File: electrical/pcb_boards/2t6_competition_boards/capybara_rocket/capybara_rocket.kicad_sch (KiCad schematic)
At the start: 77 parts, among them J1 3.6V Battery, J10 Elevator, J11 SparkFun MAX-M10S, J12 Aileron 1, J13 Aileron 2, J14 Ground Camera, J15 Payload Camera, J16 DC Motor, J2 1.2V Battery, J3 3.6V Switch, J4 1.2V Switch, J5 LED, J6 NC, J7 CC, J8 VL53L1-SATEL, J9 Egg, U1 NE555P, U10 DRV8212DRLR, U11 STM32 NUCLEO-G431KB, U12 SN74LVC1G04DBVR, U13 SparkFun XBee Explorer, U2 DS1307+, U3 Adafruit BNO085, U4 LTC3536, U5 MP3414, U6 Adafruit BMP581, U7 INA219, U8 MAX756CPA+, U9 EEPROM, Y1 AB38T-32.768KHZ

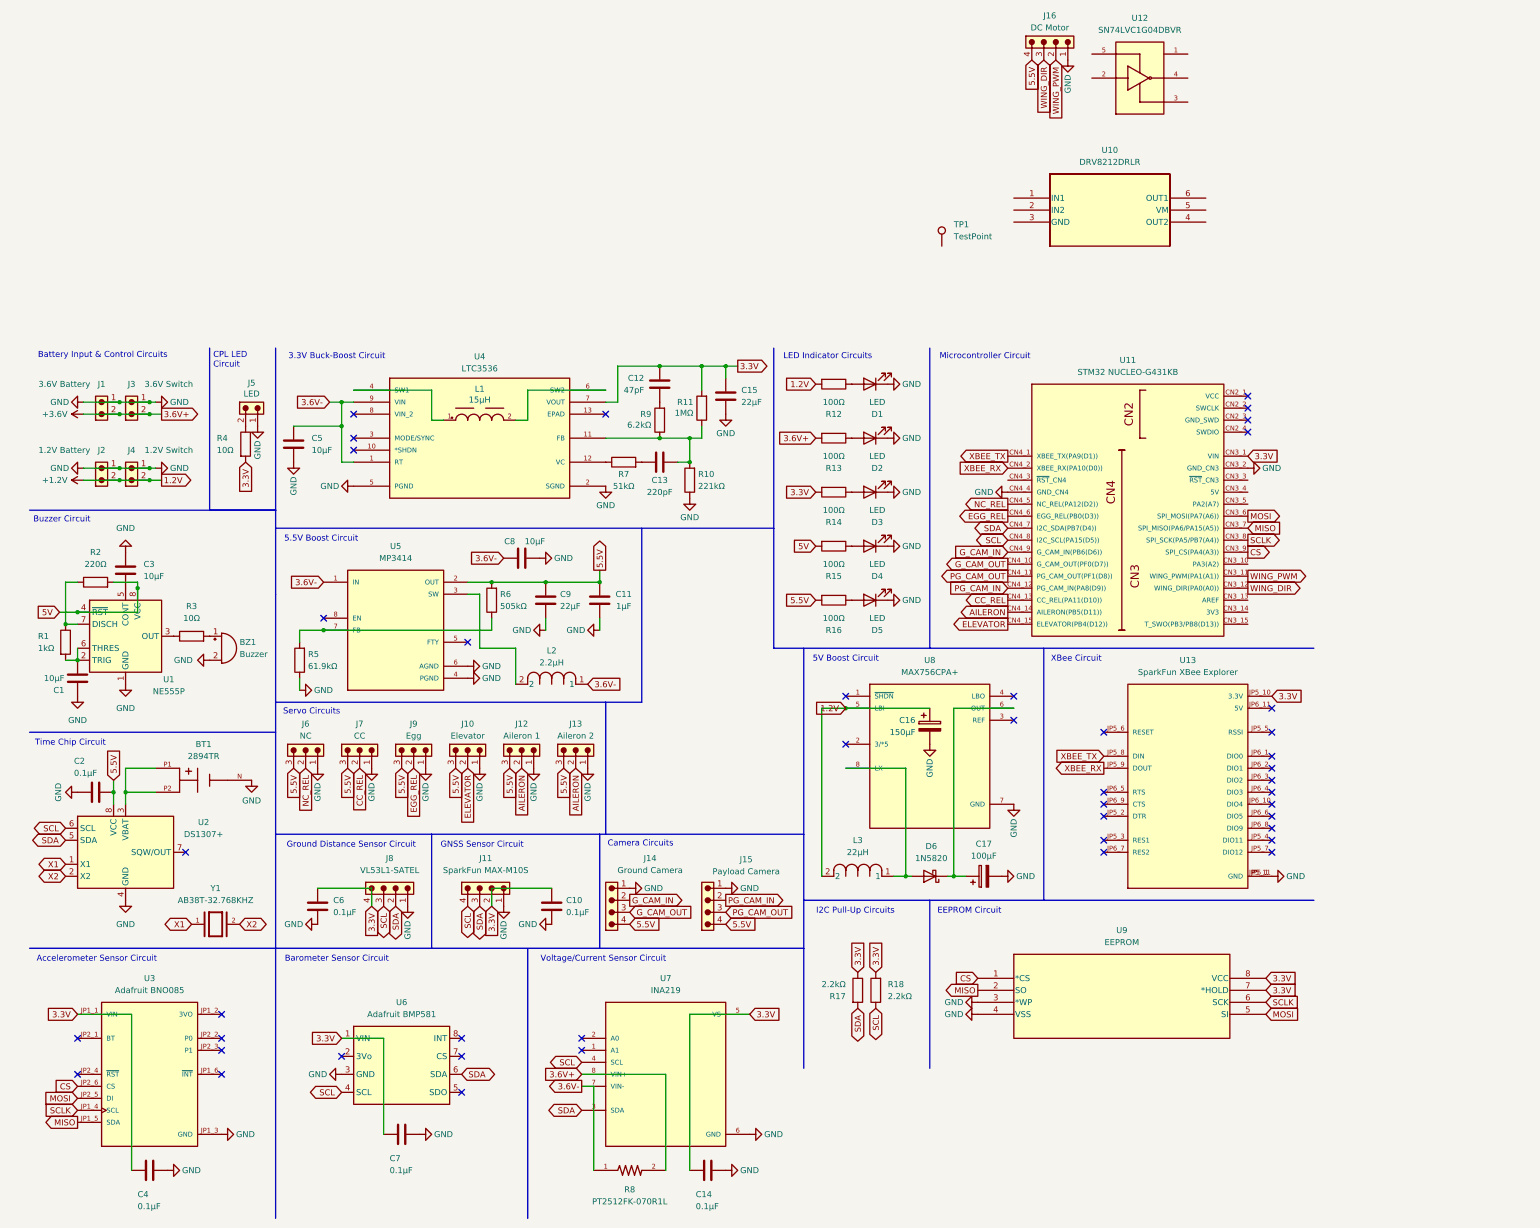
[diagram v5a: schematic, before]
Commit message: Completed CPL schematic
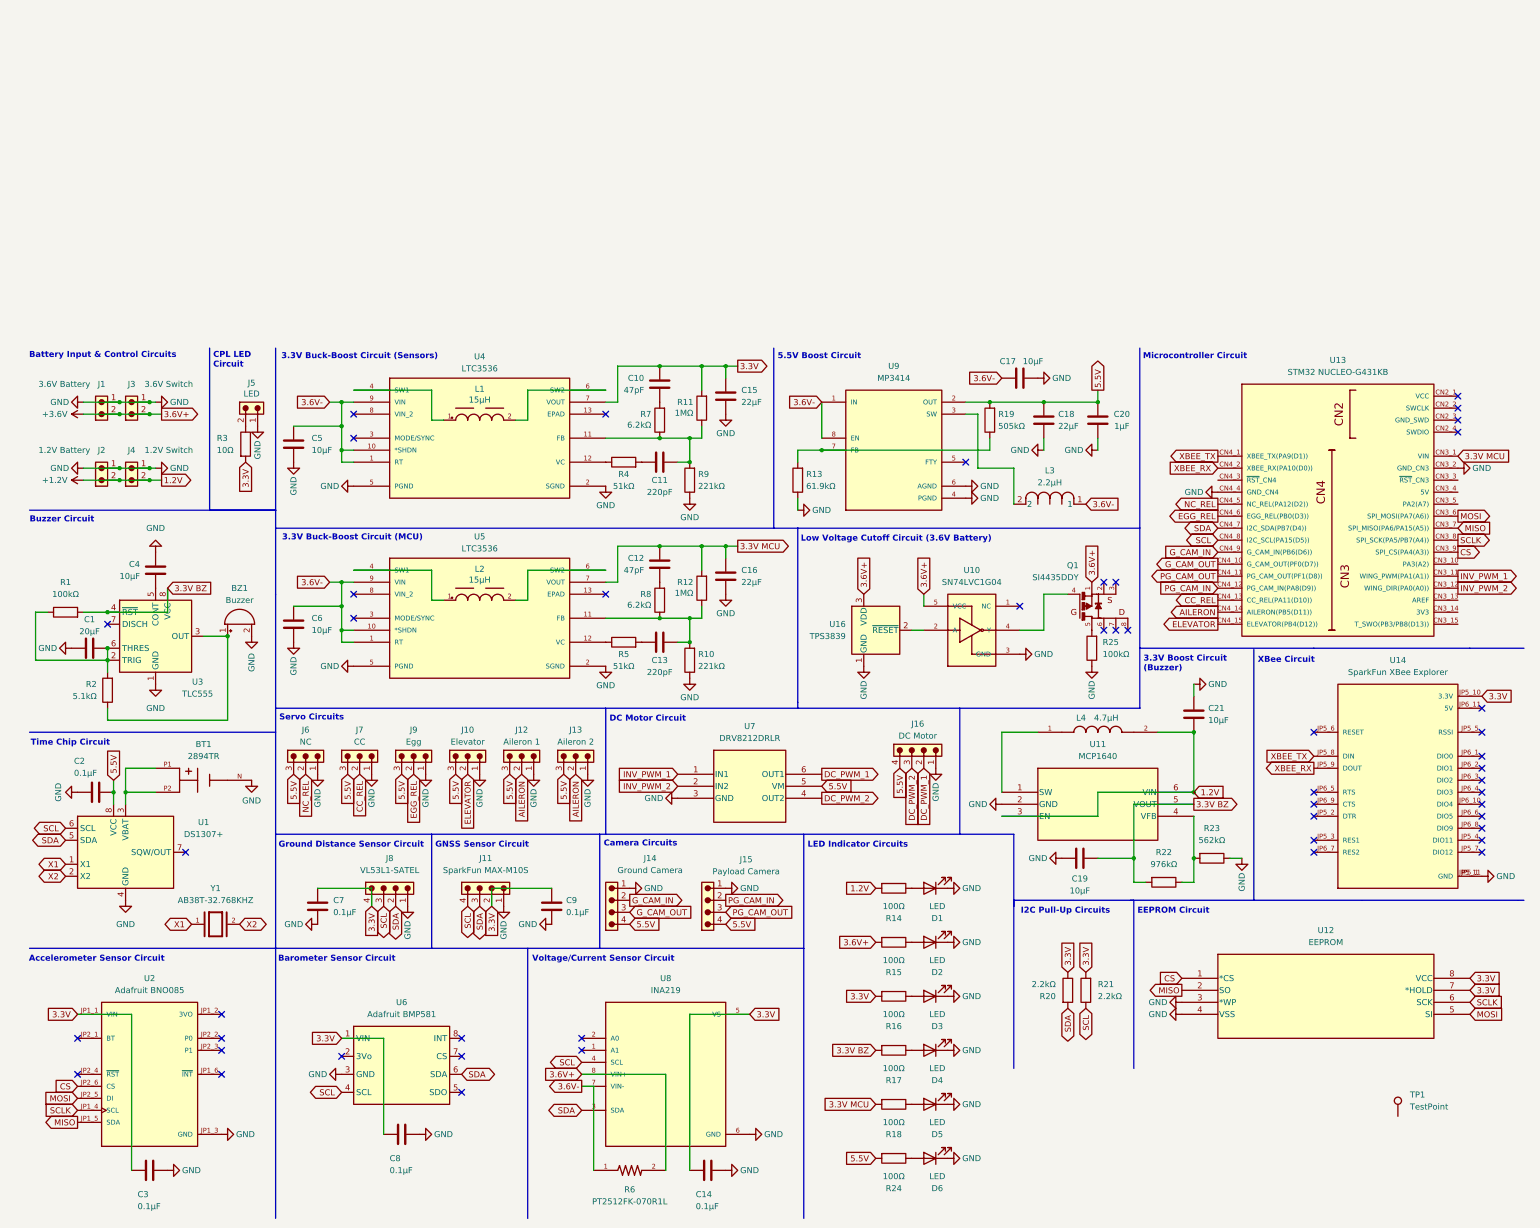
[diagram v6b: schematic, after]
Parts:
- removed C16: 150μF, Capacitor_THT:CP_Radial_D6.3mm_P2.50mm, symbol Device:C_Polarized
- removed C17: 100μF, Capacitor_THT:CP_Radial_D8.0mm_P3.50mm, symbol Device:C_Polarized
- removed C3: 10μF, Capacitor_SMD:C_0805_2012Metric_Pad1.18x1.45mm_HandSolder, symbol Device:C
- removed D6: 1N5820, Diode_THT:D_DO-201AD_P15.24mm_Horizontal, symbol Diode:1N5820
- removed L3: 22μH, RSX_CanSat_Custom_KiCad_Footprints:IND_CD54_SUM, symbol RSX_CanSat_Custom_KiCad_Symbols:CD54NP-220MC
- removed R3: 10Ω, Resistor_SMD:R_0603_1608Metric_Pad0.98x0.95mm_HandSolder, symbol Device:R
- removed U1: NE555P, Package_DIP:DIP-8_W7.62mm, symbol Timer:NE555P
- removed U8: MAX756CPA+, Package_DIP:DIP-8_W7.62mm, symbol RSX_CanSat_Custom_KiCad_Symbols:MAX756CPA_
- added C12: 47pF, Capacitor_SMD:C_0603_1608Metric_Pad1.08x0.95mm_HandSolder, symbol Device:C
- added C13: 220pF, Capacitor_SMD:C_0805_2012Metric_Pad1.18x1.45mm_HandSolder, symbol Device:C
- added C16: 22μF, Capacitor_SMD:C_0805_2012Metric_Pad1.18x1.45mm_HandSolder, symbol Device:C
- added C19, C21, C6: 10μF, Capacitor_SMD:C_1206_3216Metric_Pad1.33x1.80mm_HandSolder, symbol Device:C
- added C4: 10μF, Capacitor_SMD:C_0805_2012Metric_Pad1.18x1.45mm_HandSolder, symbol Device:C
- added D6: LED, DigiKey:WL-SMCW_0603, symbol Device:LED
- added L2: 15μH, RSX_CanSat_Custom_KiCad_Footprints:WE-TPC_4828, symbol RSX_CanSat_Custom_KiCad_Symbols:WE-TPC_4828
- added L4: 4.7μH, RSX_CanSat_Custom_KiCad_Footprints:IND_B82462G4472M000, symbol RSX_CanSat_Custom_KiCad_Symbols:B82462G4472M000
- added Q1: SI4435DDY, RSX_CanSat_Custom_KiCad_Footprints:SO-8, symbol RSX_CanSat_Custom_KiCad_Symbols:SI4435DDY
- added R10: 221kΩ, Resistor_THT:R_Axial_DIN0207_L6.3mm_D2.5mm_P7.62mm_Horizontal, symbol Device:R
- added R12: 1MΩ, Resistor_THT:R_Axial_DIN0207_L6.3mm_D2.5mm_P7.62mm_Horizontal, symbol Device:R
- added R22: 976kΩ, Resistor_SMD:R_0805_2012Metric_Pad1.20x1.40mm_HandSolder, symbol Device:R
- added R23: 562kΩ, Resistor_SMD:R_0805_2012Metric_Pad1.20x1.40mm_HandSolder, symbol Device:R
- added R24: 100Ω, Resistor_SMD:R_0603_1608Metric_Pad0.98x0.95mm_HandSolder, symbol Device:R
- added R25: 100kΩ, Resistor_THT:R_Axial_DIN0207_L6.3mm_D2.5mm_P7.62mm_Horizontal, symbol Device:R
- added R5: 51kΩ, Resistor_SMD:R_0603_1608Metric_Pad0.98x0.95mm_HandSolder, symbol Device:R
- added R8: 6.2kΩ, Resistor_SMD:R_0603_1608Metric_Pad0.98x0.95mm_HandSolder, symbol Device:R
- added U11: MCP1640, RSX_CanSat_Custom_KiCad_Footprints:SOT-23-6_MC_MCH, symbol RSX_CanSat_Custom_KiCad_Symbols:MCP1640T-I_CHY
- added U16: TPS3839, Package_TO_SOT_SMD:SOT-23, symbol Power_Supervisor:TPS3839DBZ
- added U3: TLC555, Package_DIP:DIP-8_W7.62mm, symbol Timer:TLC555xP
- added U5: LTC3536, RSX_CanSat_Custom_KiCad_Footprints:MSOP-12_MSE, symbol RSX_CanSat_Custom_KiCad_Symbols:LTC3536EMSE_PBF
- C1: value 10μF -> 20μF
- R1: value 1kΩ -> 100kΩ
- R2: value 220Ω -> 5.1kΩ
- U10: renamed from U12; value SN74LVC1G04DBVR -> SN74LVC1G04
- renumbered C12 to C10, C13 to C11, C8 to C17, C9 to C18, C11 to C20, C4 to C3, C6 to C7, C7 to C8, C10 to C9, L2 to L3, R5 to R13, R12 to R14, R13 to R15, R14 to R16, R15 to R17, R16 to R18, R6 to R19, R17 to R20, R18 to R21, R4 to R3, R7 to R4, R8 to R6, R9 to R7, R10 to R9, U2 to U1, U9 to U12, U11 to U13, U13 to U14, U3 to U2, U10 to U7, U7 to U8, U5 to U9
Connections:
- net +1.2V: now also C21.2, L4.2, U11.3 (EN), U11.6 (VIN)
- net +3.6V: now also U10.5 (VCC), Q1.1, U16.3 (VDD)
- net 3.3V: no longer U13.CN3_1 (VIN)
- net 3.6V-: now also U4.10 (*SHDN), U9.8 (EN), C6.1, U5.1 (RT), U5.10 (*SHDN), U5.9 (VIN)
- net 5.5V: now also U7.5 (VM), R24.2; no longer R18.2
- net GND: now also U10.3 (GND), U7.3 (GND), C16.1, C19.1, C21.1, C4.1, C6.2, D6.1 (K), R10.1, R23.1, R25.1, U11.2 (GND), U16.1 (GND), U3.1 (GND), U5.2 (SGND), U5.5 (PGND)
- net at R2.1: now also BZ1.1 (+), U3.3 (OUT); no longer R1.1
- net at C1.1: now also R1.1, R2.2, U3.2 (TRIG), U3.6 (THRES); no longer R1.2
- net INV_PWM_1: now reaches U7.1 (IN1)
- net INV_PWM_1: now also U13.CN3_11 (WING_PWM(PA1(A1)))
- net INV_PWM_2: now reaches U7.2 (IN2)
- net INV_PWM_2: now also U13.CN3_12 (WING_DIR(PA0(A0)))
- net DC_PWM_2: now reaches U7.4 (OUT2)
- net DC_PWM_2: now also J16.3
- net DC_PWM_1: now reaches U7.6 (OUT1)
- net DC_PWM_1: now also J16.2
- net at U10.2 (A): now also U16.2 (~{RESET})
- net at U10.4 (Y): now also Q1.4
- net 5V renamed 3.3V BZ
- net 3.3V BZ: now also R1.2, C19.2, R22.2, U11.5 (VOUT), U3.4 (~{RST}), U3.8 (VCC); no longer R2.2
- removed net WING_DIR: J16.3, U13.CN3_12 (WING_DIR(PA0(A0)))
- removed net WING_PWM: J16.2, U13.CN3_11 (WING_PWM(PA1(A1)))
- new net: C13.1, R10.2, R12.1, R8.1, U5.11 (FB)
- new net: R5.1, U5.12 (VC)
- new net: L2.1, U5.4 (SW1)
- new net: L2.2, U5.6 (SW2)
- new net: R22.1, R23.2, U11.4 (VFB)
- new net: C13.2, R5.2
- new net: Q1.5, R25.2
- new net: L4.1, U11.1 (SW)
- new net: D6.2 (A), R24.1
- new net: C4.2, U3.5 (CONT)
- new net: C12.1, R8.2
- new net 3.3V MCU: C12.2, C16.2, R12.2, R18.2, U13.CN3_1 (VIN), U5.7 (VOUT)
- no-connect marks 44 -> 48
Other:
- note added: "3.3V Boost Circuit (Buzzer)"
- note added: "3.3V Buck-Boost Circuit (MCU)"
- note added: "3.3V Buck-Boost Circuit (Sensors)"
- note added: "DC Motor Circuit"
- note added: "Low Voltage Cutoff Circuit (3.6V Battery)"
- note removed: "3.3V Buck-Boost Circuit"
- note removed: "5V Boost Circuit"
- moved on the sheet: C17, C18, C20, D1, D2, D3, D4, D5, J10, J12, J13, J16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

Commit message: Locking in sensor placements
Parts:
- Q1: footprint RSX_CanSat_Custom_KiCad_Footprints:SO-8 -> Package_SO:SOIC-8_3.9x4.9mm_P1.27mm
- renumbered R24 to R19, R19 to R20, R20 to R21, R21 to R22, R25 to R23, R22 to R24, R23 to R25, U9 to U10, U10 to U11, U11 to U12, U12 to U13, U13 to U14, U14 to U15, U16 to U9
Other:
- title: RSX Aerial CanSat 2T6 Payload PCB Design -> RSX Aerial CanSat 2T6 Payload Schematic Design

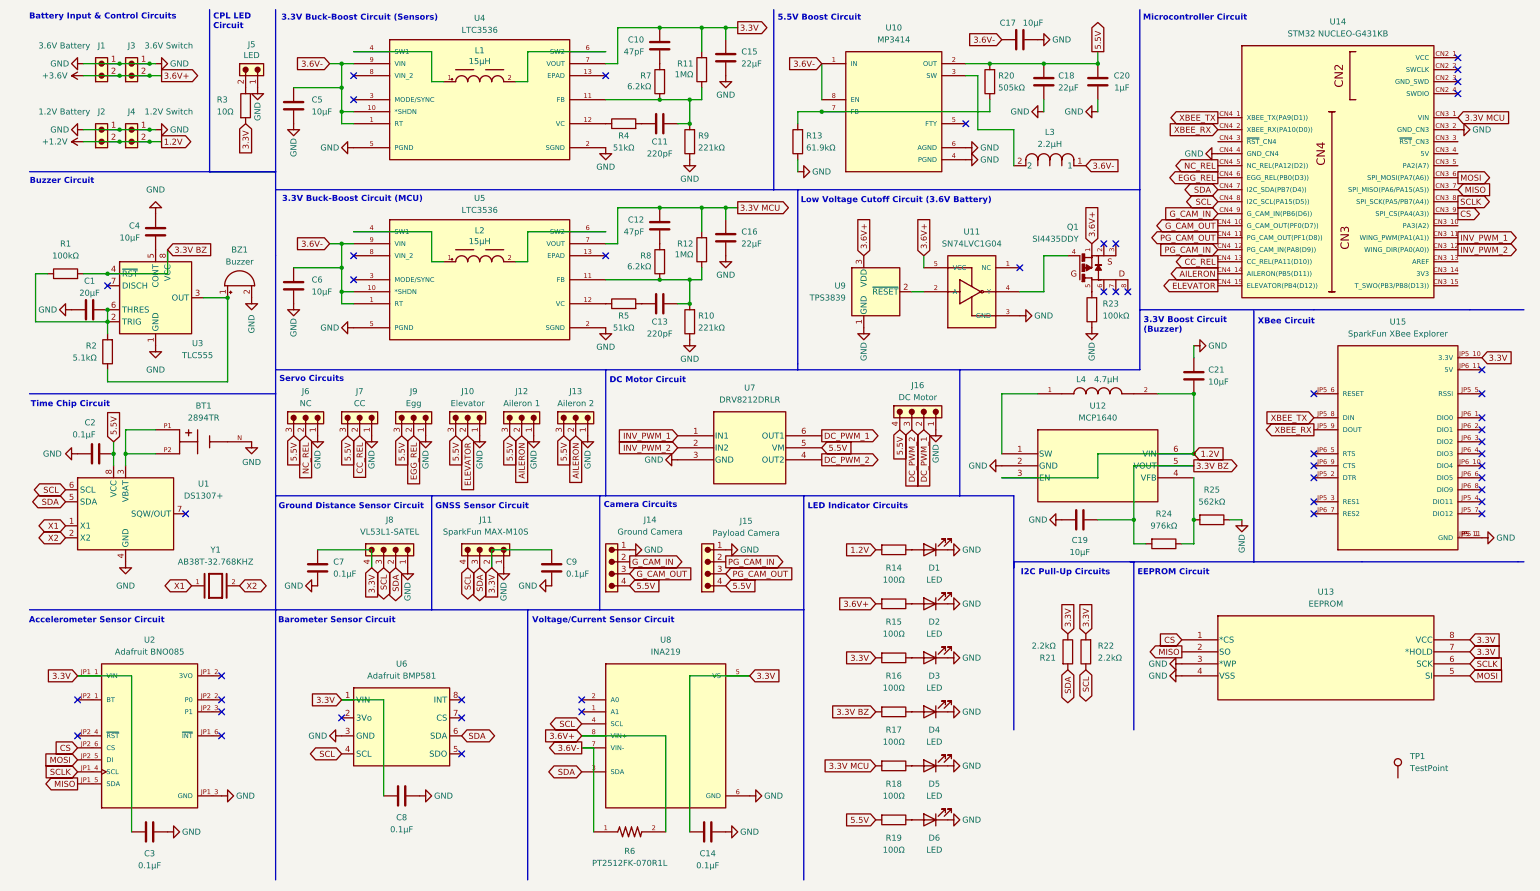
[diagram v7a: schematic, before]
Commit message: Finalized schematic design for CPL and ERC pass
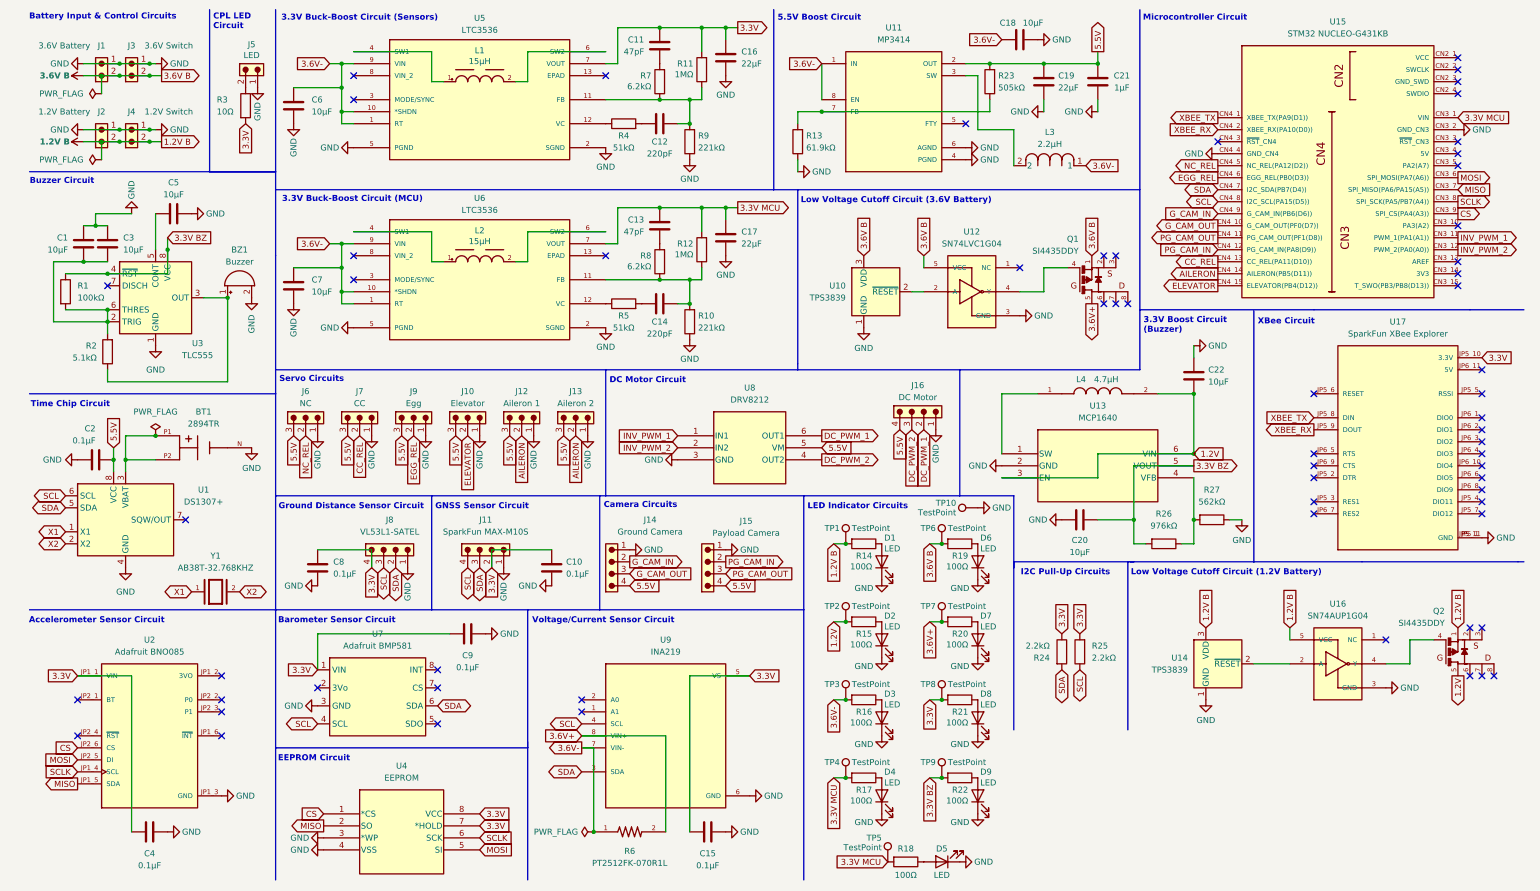
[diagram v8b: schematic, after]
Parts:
- removed R23: 100kΩ, Resistor_THT:R_Axial_DIN0207_L6.3mm_D2.5mm_P7.62mm_Horizontal, symbol Device:R
- added C3: 10μF, Capacitor_SMD:C_1206_3216Metric_Pad1.33x1.80mm_HandSolder, symbol Device:C
- added D7, D8, D9: LED, DigiKey:WL-SMCW_0603, symbol Device:LED
- added Q2: SI4435DDY, Package_SO:SOIC-8_3.9x4.9mm_P1.27mm, symbol RSX_CanSat_Custom_KiCad_Symbols:SI4435DDY
- added R20, R21, R22: 100Ω, Resistor_SMD:R_0603_1608Metric_Pad0.98x0.95mm_HandSolder, symbol Device:R
- added TP10, TP2, TP3, TP4, TP5, TP6, TP7, TP8, TP9: TestPoint, TestPoint:TestPoint_THTPad_2.0x2.0mm_Drill1.0mm, symbol Connector:TestPoint
- added U14: TPS3839, Package_TO_SOT_SMD:SOT-23-3, symbol Power_Supervisor:TPS3839DBZ
- added U16: SN74AUP1G04, Package_TO_SOT_SMD:SOT-23-5, symbol RSX_CanSat_Custom_KiCad_Symbols:SN74AUP1G04DBVR
- C1: value 20μF -> 10μF; footprint Capacitor_SMD:C_0805_2012Metric_Pad1.18x1.45mm_HandSolder -> Capacitor_SMD:C_1206_3216Metric_Pad1.33x1.80mm_HandSolder
- C5: renamed from C4; footprint Capacitor_SMD:C_0805_2012Metric_Pad1.18x1.45mm_HandSolder -> Capacitor_SMD:C_1206_3216Metric_Pad1.33x1.80mm_HandSolder
- L3: footprint IND_BOURNS_SRN6045 -> RSX_CanSat_Custom_KiCad_Footprints:IND_BOURNS_SRN6045
- TP1: footprint (none) -> TestPoint:TestPoint_THTPad_2.0x2.0mm_Drill1.0mm
- U10: renamed from U9; footprint Package_TO_SOT_SMD:SOT-23 -> Package_TO_SOT_SMD:SOT-23-3
- U12: renamed from U11; footprint RSX_CanSat_Custom_KiCad_Footprints:SOT95P280X145-5N -> Package_TO_SOT_SMD:SOT-23-5
- U8: renamed from U7; value DRV8212DRLR -> DRV8212
- U9: renamed from U8; footprint RSX_CanSat_Custom_KiCad_Footprints:SOIC127P599X175-8N -> Package_SO:SOIC-8_3.9x4.9mm_P1.27mm
- renumbered C9 to C10, C10 to C11, C11 to C12, C12 to C13, C13 to C14, C14 to C15, C15 to C16, C16 to C17, C17 to C18, C18 to C19, C19 to C20, C20 to C21, C21 to C22, C3 to C4, C5 to C6, C6 to C7, C7 to C8, C8 to C9, R20 to R23, R21 to R24, R22 to R25, R24 to R26, R25 to R27, U10 to U11, U12 to U13, U14 to U15, U15 to U17, U13 to U4, U4 to U5, U5 to U6, U6 to U7
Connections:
- net 3.3V: now also R21.2, TP8.1; no longer R16.2
- net 3.3V BZ: now also R1.1, R22.2, TP9.1; no longer R1.2, R17.2
- net 3.3V MCU: now also R17.2, TP4.1, TP5.1
- net 3.6V-: now also R16.2, TP3.1
- net 5.5V: no longer R19.2
- net GND: now also C1.1, C5.2, C3.1, D7.1 (K), D8.1 (K), D9.1 (K), TP10.1, U14.1 (GND), U16.3 (GND); no longer C1.2, C5.1
- net at R2.2, U3.2 (TRIG), U3.6 (THRES): now also C1.2, R1.2, C3.2; no longer C1.1, R1.1
- net 3.6V+: now reaches Q1.5
- net 3.6V+: now also R6.2, U9.8 (VIN+), R20.2, TP7.1
- net at U3.5 (CONT): now also C5.1; no longer C5.2
- net 1.2V B: now reaches TP1.1
- net 1.2V B: now also J2.2, J4.2, R14.2, Q2.1, U14.3 (VDD), U16.5 (VCC)
- net +1.2V renamed 1.2V
- net 1.2V: now also R15.2, Q2.5, TP2.1; no longer J2.2, J4.2, R14.2
- net +3.6V renamed 3.6V B
- net 3.6V B: now also R19.2, TP6.1; no longer R15.2, R6.2, U9.8 (VIN+)
- new net: D8.2 (A), R21.1
- new net: D7.2 (A), R20.1
- new net: U14.2 (~{RESET}), U16.2 (A)
- new net: Q2.4, U16.4 (Y)
- new net: D9.2 (A), R22.1
- no-connect marks 48 -> 62
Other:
- note added: "Low Voltage Cutoff Circuit (1.2V Battery)"
- moved on the sheet: BT1, C2, C5, C9, D1, Q1, R1, R14, R24, R25, TP1, U1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
